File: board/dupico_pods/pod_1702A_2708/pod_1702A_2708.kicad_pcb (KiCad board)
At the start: 2 copper layers, 80 x 58.4 mm, 15 parts, among them J1 dupico connector, J2 1702A, J3 2708, J4 Conn_01x06, U1 RD-0512D, U2 LM7905_TO220, U3 LM7909_TO220

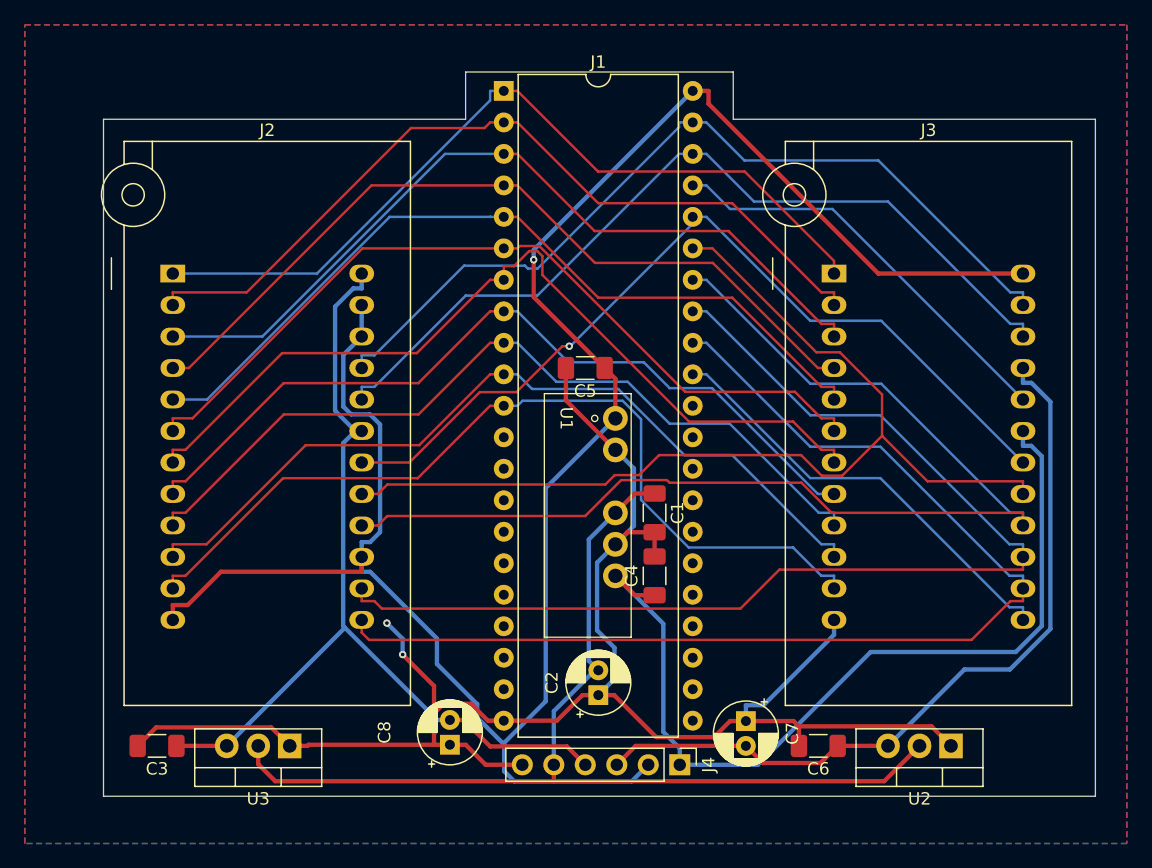
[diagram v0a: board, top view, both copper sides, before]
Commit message: Renamed 1702A pod with correct name
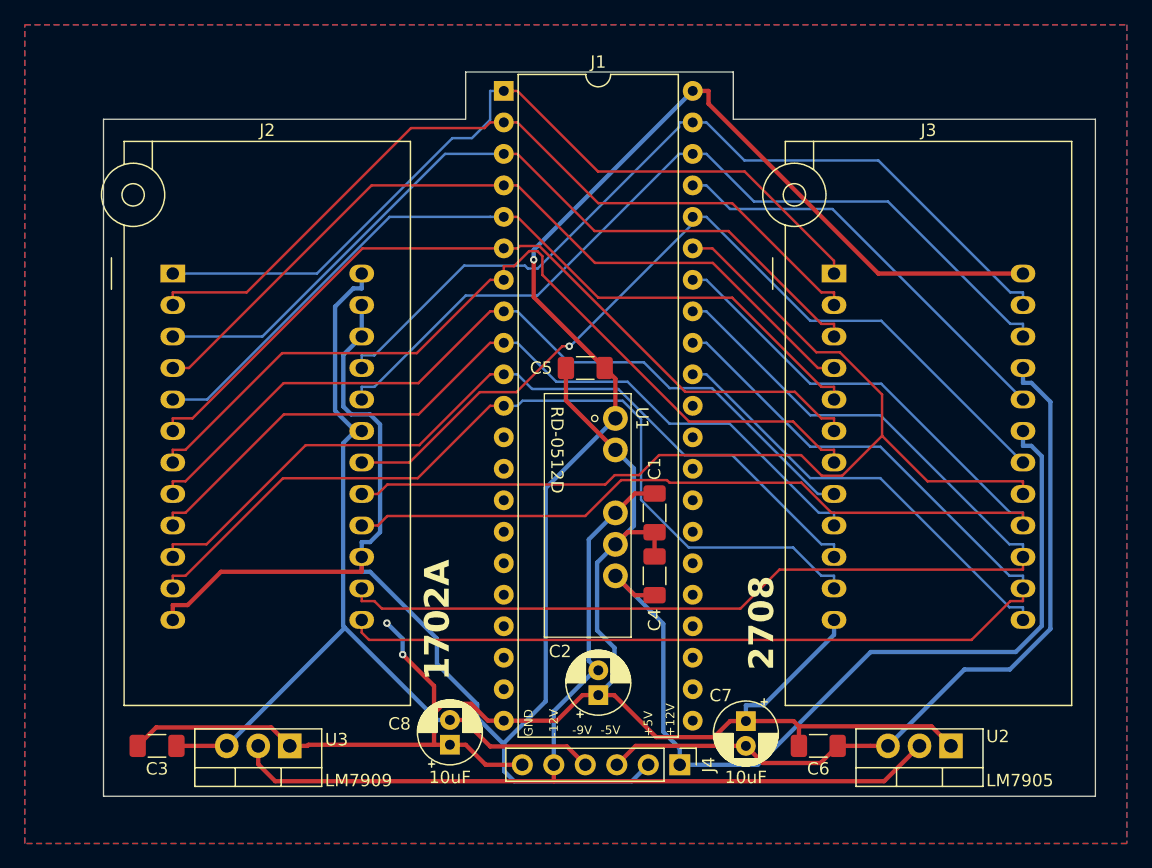
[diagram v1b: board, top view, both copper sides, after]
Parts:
- U2: value LM7905_TO220 -> LM7905
- U3: value LM7909_TO220 -> LM7909
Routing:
- net /ZIF_1: track 66.6 -> 67.5 mm
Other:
- board text added: "+12V"
- board text added: "+5V"
- board text added: "-12V"
- board text added: "-5V"
- board text added: "-9V"
- board text added: "GND"
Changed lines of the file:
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@@
 		(tags "TO-220-3 Vertical RM 2.54mm")
 		(property "Reference" "U2"
-			(at 2.54 -4.27 0)
+			(at -3.7755 0.762 0)
 			(layer "F.SilkS")
 			(effects
@@
 			)
 		)
-		(property "Value" "LM7905_TO220"
-			(at 2.54 2.5 0)
-			(layer "F.Fab")
+		(property "Value" "LM7905"
+			(at -5.5535 -2.794 0)
+			(layer "F.SilkS")
 			(effects
 				(font
@@
 		(tags "capacitor handsolder")
 		(property "Reference" "C4"
-			(at 0 -1.85 90)
+			(at -3.556 0 90)
 			(layer "F.SilkS")
 			(effects
@@
 		)
 		(property "Value" "1702A"
-			(at 7.62 35.74 0)
-			(layer "F.Fab")
+			(at 21.336 27.94 270)
+			(layer "F.SilkS")
 			(effects
 				(font
-					(size 0.6 0.6)
-					(thickness 0.09)
+					(size 2 2)
+					(thickness 0.4)
+					(bold yes)
 				)
 			)
@@
 		(tags "TO-220-3 Vertical RM 2.54mm")
 		(property "Reference" "U3"
-			(at 2.54 -4.27 0)
+			(at -3.7755 0.508 0)
 			(layer "F.SilkS")
 			(effects
@@
 			)
 		)
-		(property "Value" "LM7909_TO220"
-			(at 2.54 2.5 0)
-			(layer "F.Fab")
+		(property "Value" "LM7909"
+			(at -5.5535 -2.794 0)
+			(layer "F.SilkS")
 			(effects
 				(font
@@
 		(tags "CP Radial series Radial pin pitch 2.00mm  diameter 5mm Electrolytic Capacitor")
 		(property "Reference" "C8"
-			(at 1 -5.274 90)
+			(at 1.6882 -4.064 180)
 			(layer "F.SilkS")
 			(effects
@@
 		)
 		(property "Value" "10uF"
-			(at 1 3.75 90)
-			(layer "F.Fab")
+			(at -2.6298 0 180)
+			(layer "F.SilkS")
 			(effects
 				(font
@@
 		)
 		(property "Value" "2708"
-			(at 7.62 35.74 0)
-			(layer "F.Fab")
+			(at -5.842 28.194 90)
+			(layer "F.SilkS")
 			(effects
 				(font
-					(size 0.6 0.6)
-					(thickness 0.09)
+					(size 2 2)
+					(thickness 0.4)
+					(bold yes)
 				)
 			)
@@
 		(tags "CP Radial series Radial pin pitch 2.00mm  diameter 5mm Electrolytic Capacitor")
 		(property "Reference" "C2"
-			(at 1 -3.75 90)
+			(at 3.524 -3.0825 180)
 			(layer "F.SilkS")
 			(effects
@@
 		(at 87.63 66.04 -90)
 		(property "Reference" "U1"
-			(at 0 -0.5 -90)
+			(at 0 -6.604 -90)
 			(unlocked yes)
 			(layer "F.SilkS")
@@
 		)
 		(property "Value" "RD-0512D"
-			(at 0 1 -90)
+			(at 2.54 0.254 270)
 			(unlocked yes)
-			(layer "F.Fab")
+			(layer "F.SilkS")
 			(effects
 				(font
@@
 		(tags "capacitor handsolder")
 		(property "Reference" "C1"
-			(at 0 -1.85 90)
+			(at -3.556 0 90)
 			(layer "F.SilkS")
 			(effects
@@
 		(tags "CP Radial series Radial pin pitch 2.00mm  diameter 5mm Electrolytic Capacitor")
 		(property "Reference" "C7"
-			(at 1 -3.75 90)
+			(at -2.064 2.032 180)
 			(layer "F.SilkS")
 			(effects
@@
 		)
 		(property "Value" "10uF"
-			(at 1 3.75 90)
-			(layer "F.Fab")
+			(at 4.54 0 180)
+			(layer "F.SilkS")
 			(effects
 				(font
@@
 		(tags "capacitor handsolder")
 		(property "Reference" "C5"
-			(at 0 -1.85 0)
+			(at 3.556 0 0)
 			(layer "F.SilkS")
 			(effects
@@
 		(layer "Edge.Cuts")
 	)
+	(gr_text "+12V"
+		(at 96.52 91.694 90)
+		(layer "F.SilkS")
+		(effects
+			(font
+				(size 0.7 0.7)
+				(thickness 0.1)
+			)
+			(justify left)
+		)
+	)
+	(gr_text "-12V"
+		(at 87.122 91.694 90)
+		(layer "F.SilkS")
+		(effects
+			(font
+				(size 0.7 0.7)
+				(thickness 0.1)
+			)
+			(justify left)
+		)
+	)
+	(gr_text "-5V"
+		(at 91.694 91.186 0)
+		(layer "F.SilkS")
+		(effects
+			(font
+				(size 0.7 0.7)
+				(thickness 0.1)
+			)
+		)
+	)
+	(gr_text "+5V"
+		(at 94.742 91.694 90)
+		(layer "F.SilkS")
+		(effects
+			(font
+				(size 0.7 0.7)
+				(thickness 0.1)
+			)
+			(justify left)
+		)
+	)
+	(gr_text "GND"
+		(at 85.09 91.694 90)
+		(layer "F.SilkS")
+		(effects
+			(font
+				(size 0.7 0.7)
+				(thickness 0.1)
+			)
+			(justify left)
+		)
+	)
+	(gr_text "-9V"
+		(at 89.408 91.186 0)
+		(layer "F.SilkS")
+		(effects
+			(font
+				(size 0.7 0.7)
+				(thickness 0.1)
+			)
+		)
+	)
 	(segment
 		(start 78.2396 89.0589)
@@
 	)
 	(segment
+		(start 80.518 43.434)
+		(end 81.9858 41.9662)
+		(width 0.2)
+		(layer "B.Cu")
+		(net 14)
+	)
+	(segment
 		(start 68.0163 54.356)
-		(end 81.9858 40.3865)
+		(end 78.9383 43.434)
 		(width 0.2)
 		(layer "B.Cu")
@@
 	)
 	(segment
-		(start 83.0875 39.624)
+		(start 81.9858 39.624)
+		(end 83.0875 39.624)
+		(width 0.2)
+		(layer "B.Cu")
+		(net 14)
+	)
+	(segment
+		(start 81.9858 41.9662)
 		(end 81.9858 39.624)
 		(width 0.2)
@@
 	)
 	(segment
-		(start 56.388 54.356)
-		(end 68.0163 54.356)
+		(start 78.9383 43.434)
+		(end 80.518 43.434)
 		(width 0.2)
 		(layer "B.Cu")
@@
 	)
 	(segment
-		(start 81.9858 40.3865)
-		(end 81.9858 39.624)
+		(start 56.388 54.356)
+		(end 68.0163 54.356)
 		(width 0.2)
 		(layer "B.Cu")
